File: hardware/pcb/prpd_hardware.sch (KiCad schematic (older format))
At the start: 16 parts, among them J1 RJ45_Shielded, J11 RJ45_Shielded, J2 Conn_01x03, T1 , T2 , T3 , T4 , T5 , T6 , T7 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

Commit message: hardware: add power symbols and screenshots
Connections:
- net GND: now reaches C1.1, J1.1, J11.1, J2.1 (Pin_1), T1.1 (Pin_1), TI1.1 (Pin_1), U1.2 (~RE~), U1.3 (DE), U1.4 (DI), U1.5 (GND)
- net +3V3: now reaches C1.2, J2.3 (Pin_3), U1.8 (VCC)
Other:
- moved on the sheet: C1
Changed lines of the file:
@@
 EELAYER 30 0
 EELAYER END
-$Descr A4 11693 8268
+$Descr User 7874 5906
 encoding utf-8
 Sheet 1 1
-Title ""
-Date ""
+Title "prpd"
+Date "2021-01-28"
 Rev ""
 Comp ""
@@
 U 1 1 600DC9C0
 P 5050 3050
-F 0 "U1" V 5096 3494 50  0000 L CNN
-F 1 "SP3485EN" V 5005 3494 50  0000 L CNN
+F 0 "U1" V 5200 3400 50  0000 L CNN
+F 1 "SP3485EN" V 5300 3400 50  0000 L CNN
 F 2 "Package_SO:SOIC-8_3.9x4.9mm_P1.27mm" H 6100 2700 50  0001 C CIN
 F 3 "http://www.icbase.com/pdf/SPX/SPX00480106.pdf" H 5050 3050 50  0001 C CNN
@@
 	4550 2300 5500 2300
 Wire Wire Line
-	4250 3750 4300 3750
-Wire Wire Line
 	4550 3750 4550 3650
 Connection ~ 4550 3050
-Wire Wire Line
-	4250 3950 4300 3950
 Wire Wire Line
 	5450 3950 5450 3050
@@
 L Device:C C1
 U 1 1 60196B0E
-P 3700 3850
-F 0 "C1" H 3815 3896 50  0000 L CNN
-F 1 "0.1uF" H 3815 3805 50  0000 L CNN
-F 2 "Capacitor_SMD:C_0805_2012Metric" H 3738 3700 50  0001 C CNN
-F 3 "~" H 3700 3850 50  0001 C CNN
-	1    3700 3850
-	1    0    0    -1
-$EndComp
-Wire Wire Line
-	4300 3750 4300 3500
-Wire Wire Line
-	4300 3500 3700 3500
-Wire Wire Line
-	3700 3500 3700 3700
-Connection ~ 4300 3750
-Wire Wire Line
-	4300 3750 4550 3750
-Wire Wire Line
-	3700 4000 3700 4150
-Wire Wire Line
-	3700 4150 4300 4150
-Wire Wire Line
-	4300 4150 4300 3950
-Connection ~ 4300 3950
-Wire Wire Line
-	4300 3950 5450 3950
+P 6450 2950
+F 0 "C1" H 6565 2996 50  0000 L CNN
+F 1 "0.1uF" H 6565 2905 50  0000 L CNN
+F 2 "Capacitor_SMD:C_0805_2012Metric" H 6488 2800 50  0001 C CNN
+F 3 "~" H 6450 2950 50  0001 C CNN
+	1    6450 2950
+	-1   0    0    1
+$EndComp
+$Comp
+L power:+3.3V #PWR?
+U 1 1 6012BA68
+P 5650 3050
+F 0 "#PWR?" H 5650 2900 50  0001 C CNN
+F 1 "+3.3V" H 5650 3000 50  0000 C CNN
+F 2 "" H 5650 3050 50  0001 C CNN
+F 3 "" H 5650 3050 50  0001 C CNN
+	1    5650 3050
+	1    0    0    -1
+$EndComp
+$Comp
+L power:GND #PWR?
+U 1 1 6012C273
+P 4350 3100
+F 0 "#PWR?" H 4350 2850 50  0001 C CNN
+F 1 "GND" H 4355 2927 50  0000 C CNN
+F 2 "" H 4350 3100 50  0001 C CNN
+F 3 "" H 4350 3100 50  0001 C CNN
+	1    4350 3100
+	1    0    0    -1
+$EndComp
+Wire Wire Line
+	4550 3050 4350 3050
+Wire Wire Line
+	4350 3050 4350 3100
+Wire Wire Line
+	5650 3050 5450 3050
+Connection ~ 5450 3050
+$Comp
+L power:GND #PWR?
+U 1 1 6013FDD2
+P 6450 3100
+F 0 "#PWR?" H 6450 2850 50  0001 C CNN
+F 1 "GND" H 6455 2927 50  0000 C CNN
+F 2 "" H 6450 3100 50  0001 C CNN
+F 3 "" H 6450 3100 50  0001 C CNN
+	1    6450 3100
+	1    0    0    -1
+$EndComp
+$Comp
+L power:+3.3V #PWR?
+U 1 1 60144A80
+P 6450 2800
+F 0 "#PWR?" H 6450 2650 50  0001 C CNN
+F 1 "+3.3V" H 6450 2750 50  0000 C CNN
+F 2 "" H 6450 2800 50  0001 C CNN
+F 3 "" H 6450 2800 50  0001 C CNN
+	1    6450 2800
+	1    0    0    -1
+$EndComp
+Wire Wire Line
+	4250 3750 4550 3750
+Wire Wire Line
+	4250 3950 5450 3950
 $EndSCHEMATC

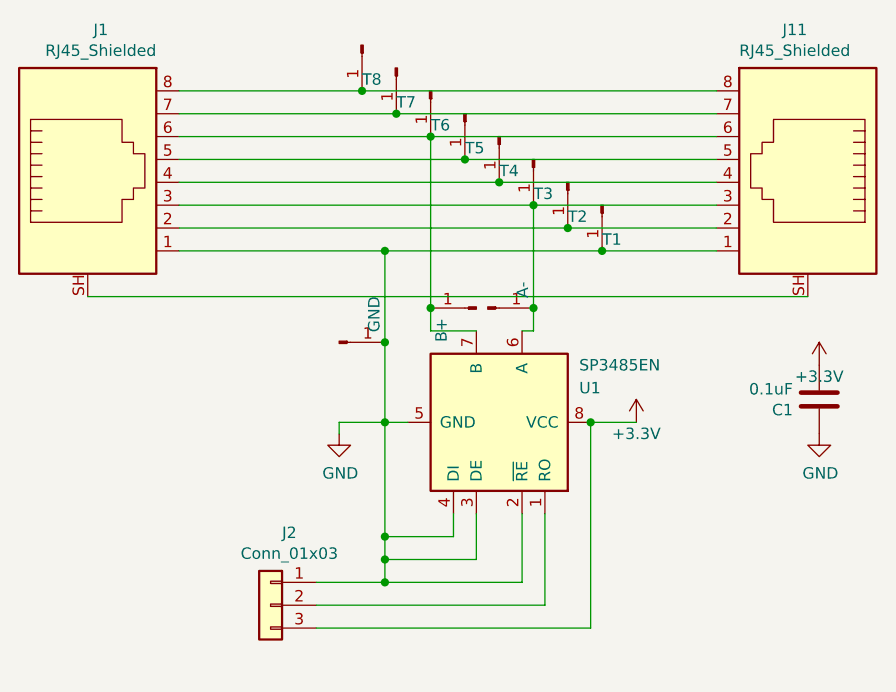
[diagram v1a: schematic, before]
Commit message: fix mixup of datalines
datalines of transceivers do swap A and B. the relevant information is
+/- or non inverting/inverting. serial ttl output was inverted; readings
where broken, most symbols where around 255.
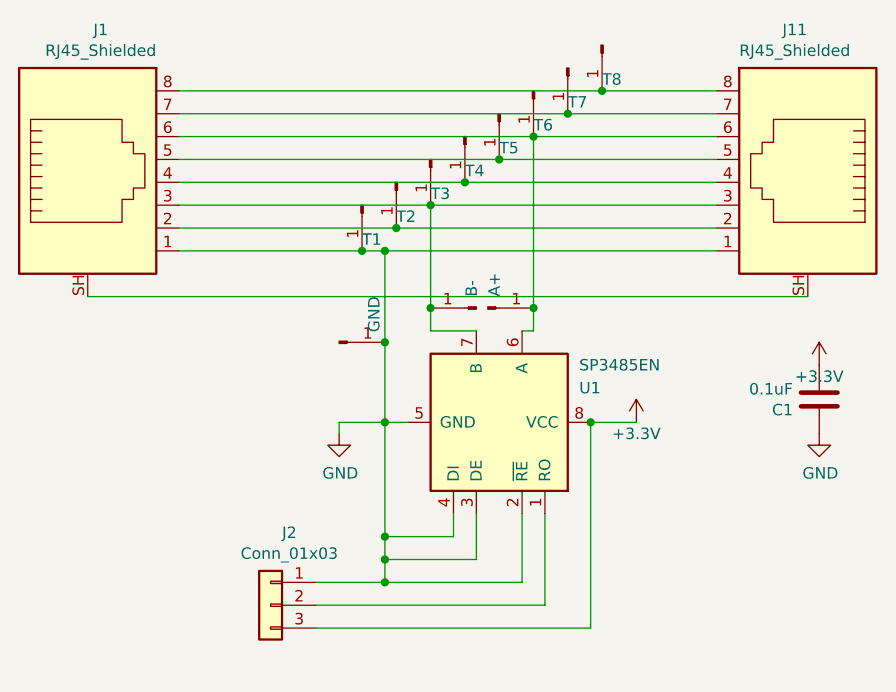
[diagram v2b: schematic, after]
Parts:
- TI2: value A- -> A+
- TI3: value B+ -> B-
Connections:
- net at J1.3, J11.3, T3.1 (Pin_1): now also TI3.1 (Pin_1), U1.7 (B); no longer TI2.1 (Pin_1), U1.6 (A)
- net at J1.6, J11.6, T6.1 (Pin_1): now also TI2.1 (Pin_1), U1.6 (A); no longer TI3.1 (Pin_1), U1.7 (B)
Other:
- moved on the sheet: T1, T2, T3, T4, T5, T6, T7, T8
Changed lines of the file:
@@
 L Connector:Conn_01x01_Male T8
 U 1 1 600D90A9
-P 4450 1400
-F 0 "T8" V 4600 1400 50  0000 L CNN
-F 1 " " V 4603 1444 50  0000 L CNN
-F 2 "prpd_hardware:tab" H 4450 1400 50  0001 C CNN
-F 3 "~" H 4450 1400 50  0001 C CNN
-	1    4450 1400
+P 5500 1400
+F 0 "T8" V 5650 1400 50  0000 L CNN
+F 1 " " V 5653 1444 50  0000 L CNN
+F 2 "prpd_hardware:tab" H 5500 1400 50  0001 C CNN
+F 3 "~" H 5500 1400 50  0001 C CNN
+	1    5500 1400
 	0    1    1    0
 $EndComp
@@
 L Connector:Conn_01x01_Male T7
 U 1 1 600DA03B
-P 4600 1500
-F 0 "T7" V 4750 1500 50  0000 L CNN
-F 1 " " V 4753 1544 50  0000 L CNN
-F 2 "prpd_hardware:tab" H 4600 1500 50  0001 C CNN
-F 3 "~" H 4600 1500 50  0001 C CNN
-	1    4600 1500
+P 5350 1500
+F 0 "T7" V 5500 1500 50  0000 L CNN
+F 1 " " V 5503 1544 50  0000 L CNN
+F 2 "prpd_hardware:tab" H 5350 1500 50  0001 C CNN
+F 3 "~" H 5350 1500 50  0001 C CNN
+	1    5350 1500
 	0    1    1    0
 $EndComp
@@
 L Connector:Conn_01x01_Male T6
 U 1 1 600DA6BC
-P 4750 1600
-F 0 "T6" V 4900 1600 50  0000 L CNN
-F 1 " " V 4903 1644 50  0000 L CNN
-F 2 "prpd_hardware:tab" H 4750 1600 50  0001 C CNN
-F 3 "~" H 4750 1600 50  0001 C CNN
-	1    4750 1600
+P 5200 1600
+F 0 "T6" V 5350 1600 50  0000 L CNN
+F 1 " " V 5353 1644 50  0000 L CNN
+F 2 "prpd_hardware:tab" H 5200 1600 50  0001 C CNN
+F 3 "~" H 5200 1600 50  0001 C CNN
+	1    5200 1600
 	0    1    1    0
 $EndComp
@@
 L Connector:Conn_01x01_Male T5
 U 1 1 600DAA20
-P 4900 1700
-F 0 "T5" V 5050 1700 50  0000 L CNN
-F 1 " " V 5053 1744 50  0000 L CNN
-F 2 "prpd_hardware:tab" H 4900 1700 50  0001 C CNN
-F 3 "~" H 4900 1700 50  0001 C CNN
-	1    4900 1700
+P 5050 1700
+F 0 "T5" V 5200 1700 50  0000 L CNN
+F 1 " " V 5203 1744 50  0000 L CNN
+F 2 "prpd_hardware:tab" H 5050 1700 50  0001 C CNN
+F 3 "~" H 5050 1700 50  0001 C CNN
+	1    5050 1700
 	0    1    1    0
 $EndComp
@@
 L Connector:Conn_01x01_Male T4
 U 1 1 600DAF87
-P 5050 1800
-F 0 "T4" V 5200 1800 50  0000 L CNN
-F 1 " " V 5203 1844 50  0000 L CNN
-F 2 "prpd_hardware:tab" H 5050 1800 50  0001 C CNN
-F 3 "~" H 5050 1800 50  0001 C CNN
-	1    5050 1800
+P 4900 1800
+F 0 "T4" V 5050 1800 50  0000 L CNN
+F 1 " " V 5053 1844 50  0000 L CNN
+F 2 "prpd_hardware:tab" H 4900 1800 50  0001 C CNN
+F 3 "~" H 4900 1800 50  0001 C CNN
+	1    4900 1800
 	0    1    1    0
 $EndComp
@@
 L Connector:Conn_01x01_Male T3
 U 1 1 600DB38E
-P 5200 1900
-F 0 "T3" V 5350 1900 50  0000 L CNN
-F 1 " " V 5353 1944 50  0000 L CNN
-F 2 "prpd_hardware:tab" H 5200 1900 50  0001 C CNN
-F 3 "~" H 5200 1900 50  0001 C CNN
-	1    5200 1900
+P 4750 1900
+F 0 "T3" V 4900 1900 50  0000 L CNN
+F 1 " " V 4903 1944 50  0000 L CNN
+F 2 "prpd_hardware:tab" H 4750 1900 50  0001 C CNN
+F 3 "~" H 4750 1900 50  0001 C CNN
+	1    4750 1900
 	0    1    1    0
 $EndComp
@@
 L Connector:Conn_01x01_Male T2
 U 1 1 600DB7D2
-P 5350 2000
-F 0 "T2" V 5500 2000 50  0000 L CNN
-F 1 " " V 5503 2044 50  0000 L CNN
-F 2 "prpd_hardware:tab" H 5350 2000 50  0001 C CNN
-F 3 "~" H 5350 2000 50  0001 C CNN
-	1    5350 2000
+P 4600 2000
+F 0 "T2" V 4750 2000 50  0000 L CNN
+F 1 " " V 4753 2044 50  0000 L CNN
+F 2 "prpd_hardware:tab" H 4600 2000 50  0001 C CNN
+F 3 "~" H 4600 2000 50  0001 C CNN
+	1    4600 2000
 	0    1    1    0
 $EndComp
@@
 L Connector:Conn_01x01_Male T1
 U 1 1 600DBB38
-P 5500 2100
-F 0 "T1" V 5650 2100 50  0000 L CNN
-F 1 " " V 5653 2144 50  0000 L CNN
-F 2 "prpd_hardware:tab" H 5500 2100 50  0001 C CNN
-F 3 "~" H 5500 2100 50  0001 C CNN
-	1    5500 2100
+P 4450 2100
+F 0 "T1" V 4600 2100 50  0000 L CNN
+F 1 " " V 4603 2144 50  0000 L CNN
+F 2 "prpd_hardware:tab" H 4450 2100 50  0001 C CNN
+F 3 "~" H 4450 2100 50  0001 C CNN
+	1    4450 2100
 	0    1    1    0
 $EndComp
@@
 $EndComp
 Wire Wire Line
-	3650 1600 4450 1600
-Wire Wire Line
-	6000 1700 4600 1700
-Wire Wire Line
-	3650 1800 4750 1800
-Wire Wire Line
-	6000 1900 4900 1900
-Wire Wire Line
-	3650 2000 5050 2000
-Wire Wire Line
-	6000 2100 5200 2100
-Wire Wire Line
-	3650 2200 5350 2200
-Wire Wire Line
-	6000 2300 5500 2300
-Connection ~ 4450 1600
-Wire Wire Line
-	4450 1600 6000 1600
-Connection ~ 4600 1700
-Wire Wire Line
-	4600 1700 3650 1700
-Connection ~ 4750 1800
-Wire Wire Line
-	4750 1800 6000 1800
-Connection ~ 4900 1900
-Wire Wire Line
-	4900 1900 3650 1900
-Connection ~ 5050 2000
-Wire Wire Line
-	5050 2000 6000 2000
-Connection ~ 5200 2100
-Wire Wire Line
-	5200 2100 3650 2100
-Connection ~ 5350 2200
-Wire Wire Line
-	5350 2200 6000 2200
-Connection ~ 5500 2300
-Wire Wire Line
-	3650 2300 4550 2300
+	6000 1700 5350 1700
+Wire Wire Line
+	6000 1900 5050 1900
+Wire Wire Line
+	3650 2300 4450 2300
 Wire Wire Line
 	5150 2650 5200 2650
 Wire Wire Line
 	5200 2650 5200 2550
-Wire Wire Line
-	4950 2650 4750 2650
 Wire Wire Line
 	4750 2650 4750 2550
@@
 	4550 3050 4650 3050
 Connection ~ 4550 2300
-Wire Wire Line
-	4550 2300 5500 2300
 Wire Wire Line
 	4550 3750 4550 3650
@@
 P 5000 2550
 F 0 "TI2" V 5150 2550 50  0001 L CNN
-F 1 "A-" V 5153 2594 50  0000 L CNN
+F 1 "A+" V 5000 2600 50  0000 L TNN
 F 2 "prpd_hardware:tab" H 5000 2550 50  0001 C CNN
 F 3 "~" H 5000 2550 50  0001 C CNN
@@
 P 4950 2550
 F 0 "TI3" V 5100 2550 50  0001 L CNN
-F 1 "B+" V 5103 2594 50  0000 L CNN
+F 1 "B-" V 5000 2500 50  0000 R BNN
 F 2 "prpd_hardware:tab" H 4950 2550 50  0001 C CNN
 F 3 "~" H 4950 2550 50  0001 C CNN
@@
 Wire Wire Line
 	4550 2700 4550 3050
-Connection ~ 4750 2550
-Wire Wire Line
-	4750 2550 4750 1800
-Connection ~ 5200 2550
-Wire Wire Line
-	5200 2550 5200 2100
 $Comp
 L Device:C C1
@@
 $EndComp
 $Comp
-L power:+3.3V #PWR?
+L power:+3.3V #PWR0101
 U 1 1 6012BA68
 P 5650 3050
-F 0 "#PWR?" H 5650 2900 50  0001 C CNN
+F 0 "#PWR0101" H 5650 2900 50  0001 C CNN
 F 1 "+3.3V" H 5650 3000 50  0000 C CNN
 F 2 "" H 5650 3050 50  0001 C CNN
@@
 $EndComp
 $Comp
-L power:GND #PWR?
+L power:GND #PWR0102
 U 1 1 6012C273
 P 4350 3100
-F 0 "#PWR?" H 4350 2850 50  0001 C CNN
+F 0 "#PWR0102" H 4350 2850 50  0001 C CNN
 F 1 "GND" H 4355 2927 50  0000 C CNN
 F 2 "" H 4350 3100 50  0001 C CNN
@@
 Connection ~ 5450 3050
 $Comp
-L power:GND #PWR?
+L power:GND #PWR0103
 U 1 1 6013FDD2
 P 6450 3100
-F 0 "#PWR?" H 6450 2850 50  0001 C CNN
+F 0 "#PWR0103" H 6450 2850 50  0001 C CNN
 F 1 "GND" H 6455 2927 50  0000 C CNN
 F 2 "" H 6450 3100 50  0001 C CNN
@@
 $EndComp
 $Comp
-L power:+3.3V #PWR?
+L power:+3.3V #PWR0104
 U 1 1 60144A80
 P 6450 2800
-F 0 "#PWR?" H 6450 2650 50  0001 C CNN
+F 0 "#PWR0104" H 6450 2650 50  0001 C CNN
 F 1 "+3.3V" H 6450 2750 50  0000 C CNN
 F 2 "" H 6450 2800 50  0001 C CNN
@@
 Wire Wire Line
 	4250 3950 5450 3950
+Connection ~ 4450 2300
+Wire Wire Line
+	4450 2300 4550 2300
+Connection ~ 5500 1600
+Wire Wire Line
+	5500 1600 6000 1600
+Connection ~ 5350 1700
+Connection ~ 5200 1800
+Wire Wire Line
+	5200 1800 6000 1800
+Connection ~ 5050 1900
+Connection ~ 4900 2000
+Connection ~ 4750 2100
+Connection ~ 4600 2200
+Wire Wire Line
+	4550 2300 6000 2300
+Wire Wire Line
+	4600 2200 6000 2200
+Wire Wire Line
+	4750 2100 6000 2100
+Wire Wire Line
+	4900 2000 6000 2000
+Wire Wire Line
+	3650 1800 5200 1800
+Wire Wire Line
+	3650 1900 5050 1900
+Wire Wire Line
+	3650 2000 4900 2000
+Wire Wire Line
+	3650 2100 4750 2100
+Wire Wire Line
+	3650 2200 4600 2200
+Connection ~ 4750 2550
+Wire Wire Line
+	4750 2550 4750 2100
+Wire Wire Line
+	3650 1600 5500 1600
+Wire Wire Line
+	3650 1700 5350 1700
+Wire Wire Line
+	5200 2550 5200 1800
+Connection ~ 5200 2550
+Wire Wire Line
+	4950 2650 4750 2650
 $EndSCHEMATC
